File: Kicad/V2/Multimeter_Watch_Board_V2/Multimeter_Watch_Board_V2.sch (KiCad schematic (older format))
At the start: 50 parts, among them J1 S3B-PH-K-S(LF)(SN), J2 S3B-PH-K-S(LF)(SN), J3 S3B-PH-K-S(LF)(SN), J6 51281-1294, J7 Conn_01x11_Female, J8 Conn_01x11_Female, Q1 A03400A N-MOS, U1 PCF85163-SO08, U2 AD8592, Y1 32kHz

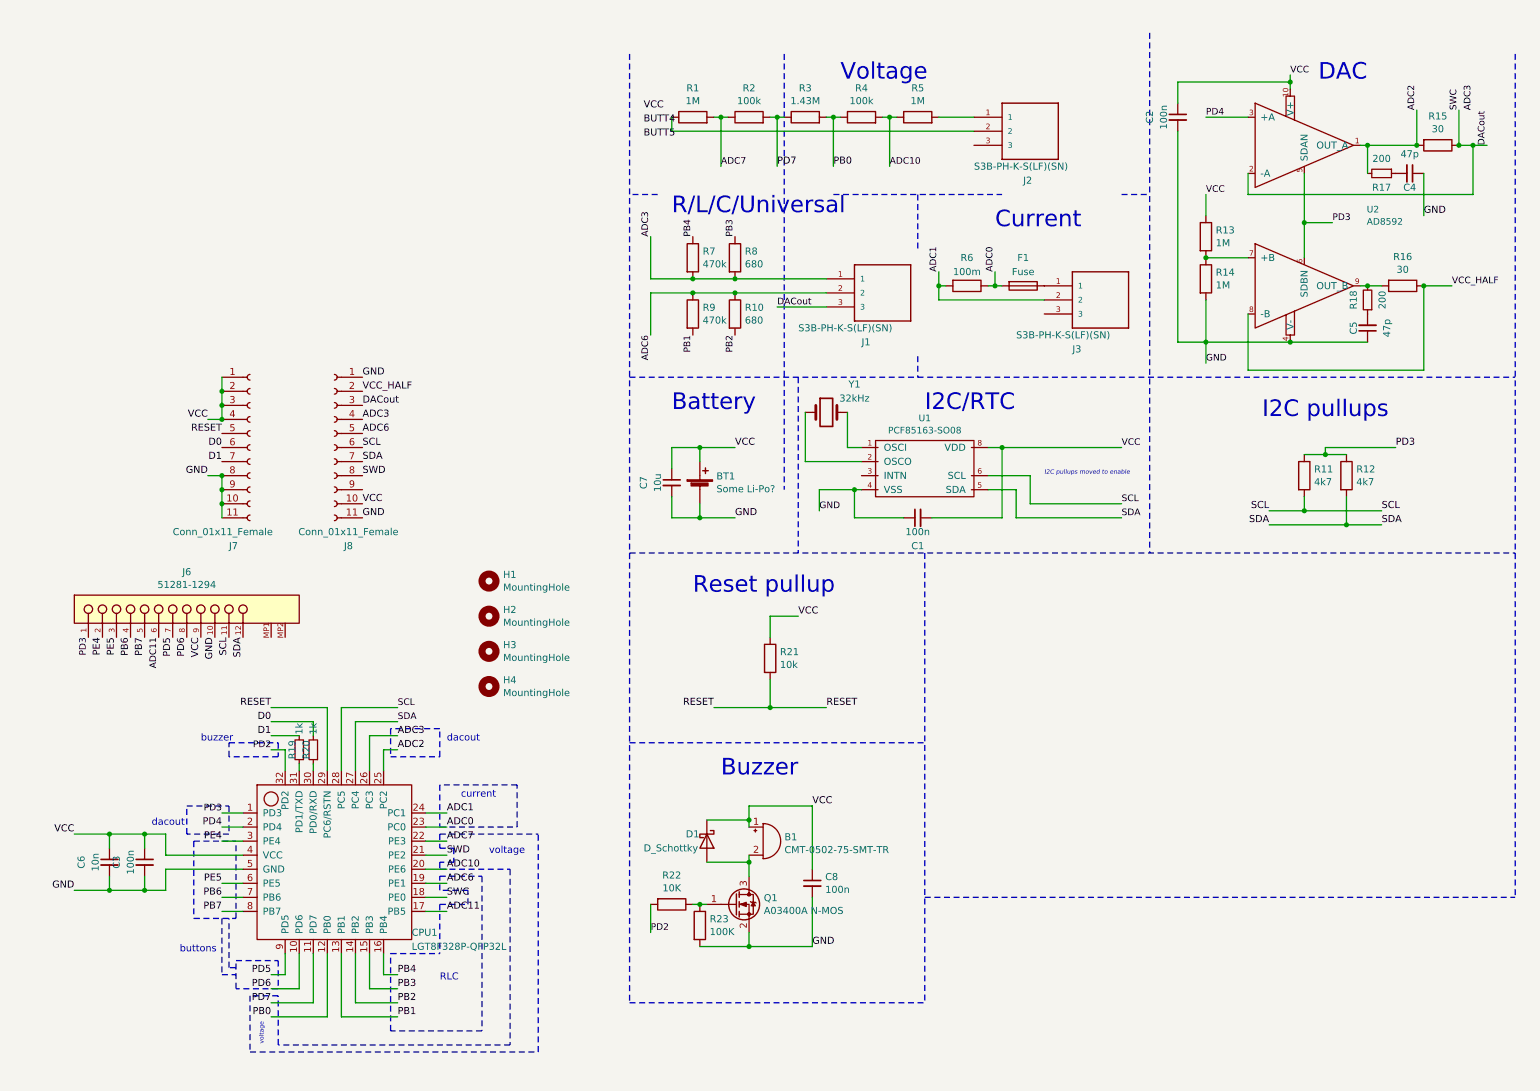
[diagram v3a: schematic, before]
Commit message: clean up schematic
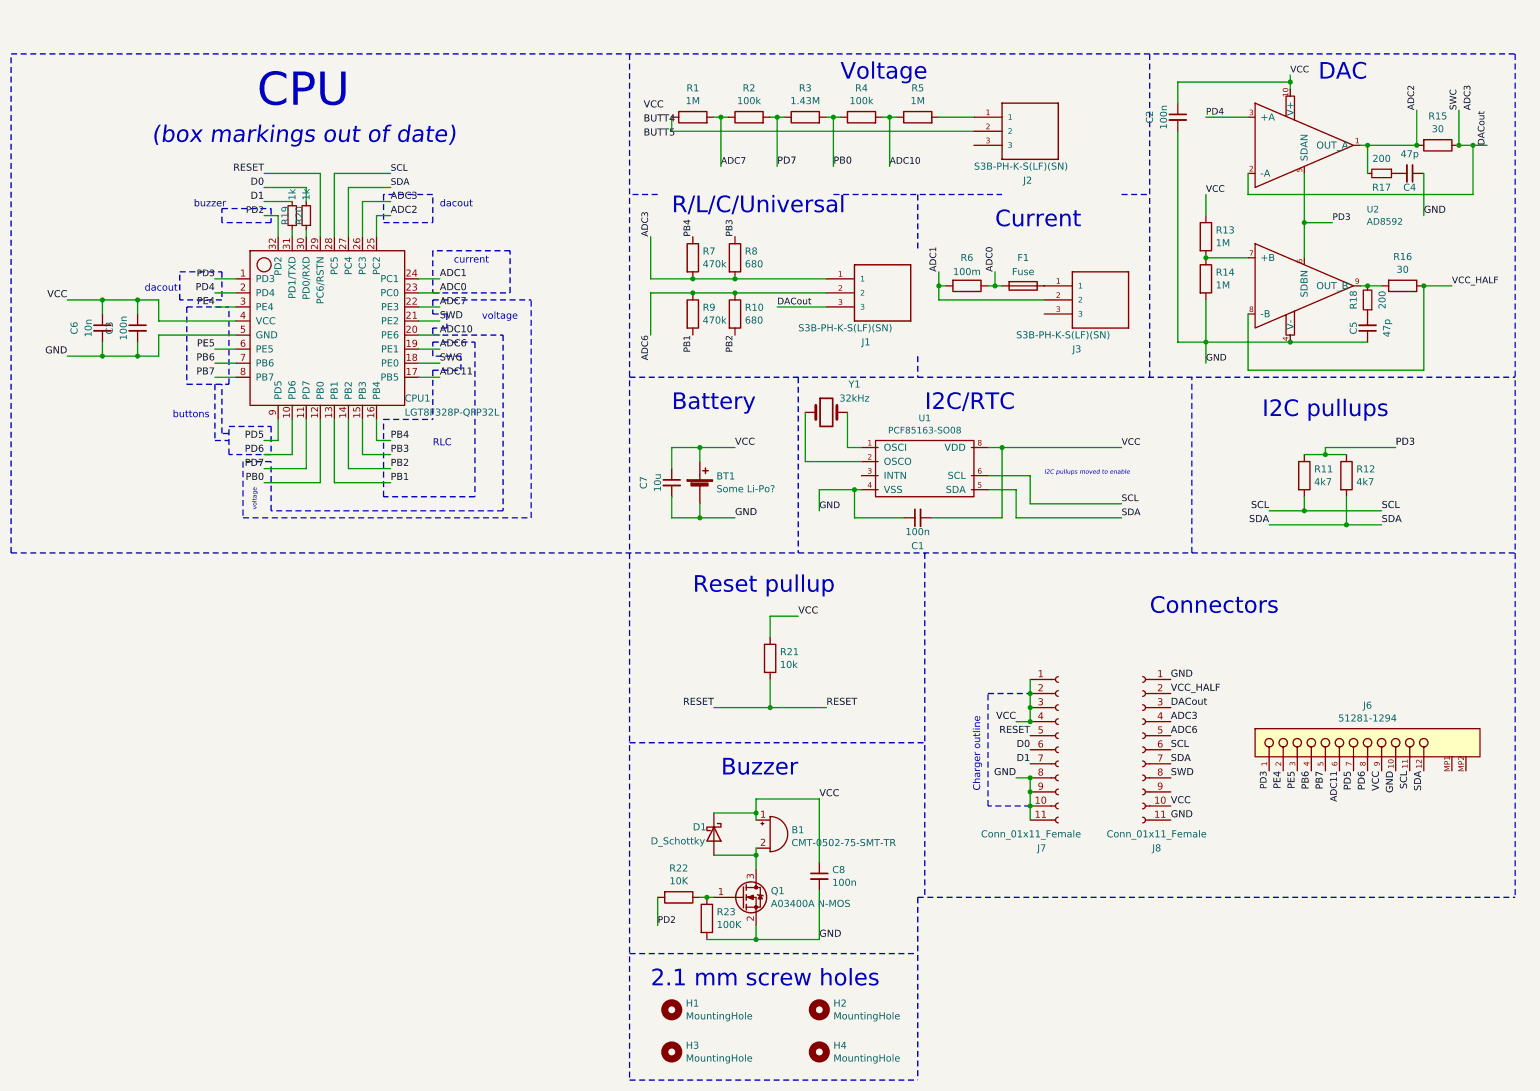
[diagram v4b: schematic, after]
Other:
- note added: "(box markings out of date)"
- note added: "2.1 mm screw holes"
- note added: "CPU"
- note added: "Charger outline"
- note added: "Connectors"
- moved on the sheet: B1, C3, C6, C8, CPU1, D1, H1, H2, H3, H4, J6, J7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

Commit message: displayboard layout for V2
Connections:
- net GND: now also J6.9
- net VCC: no longer J6.9
- net ADC11 renamed PB5
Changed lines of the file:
@@
 ADC10
 Text Label 3550 2800 0    50   ~ 0
-ADC11
+PB5
 Text Label 3550 2200 0    50   ~ 0
 ADC0
@@
 Text Label 9850 5600 3    50   ~ 0
 PB7
-Text Label 10250 5600 3    50   ~ 0
-VCC
 Text Label 9650 5600 3    50   ~ 0
 PE5
@@
 PD3
 Text Label 9950 5600 3    47   ~ 0
-ADC11
+PB5
 Wire Wire Line
 	5800 5800 6250 5800
@@
 Wire Notes Line
 	500  500  11200 500
+Text Label 10250 5600 3    50   ~ 0
+GND
 $EndSCHEMATC

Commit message: females layout improvements, add silkscreen labels for female pins
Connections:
- net DACout: now also J8.6 (Pin_6); no longer J8.3 (Pin_3)
- net SCL: now also J8.8 (Pin_8); no longer J8.6 (Pin_6)
- net SDA: now also J8.9 (Pin_9); no longer J8.7 (Pin_7)
- net SWD: now also J8.7 (Pin_7); no longer J8.8 (Pin_8)
- net VCC: now also J8.2 (Pin_2)
- net VCC_HALF: now also J8.3 (Pin_3); no longer J8.2 (Pin_2)
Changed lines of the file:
@@
 Text Label 8750 4950 0    50   ~ 0
 GND
-Text Label 8750 5050 0    50   ~ 0
+Text Label 8750 5150 0    50   ~ 0
 VCC_HALF
-Text Label 8750 5150 0    50   ~ 0
+Text Label 8750 5450 0    50   ~ 0
 DACout
-Text Label 8750 5650 0    50   ~ 0
+Text Label 8750 5550 0    50   ~ 0
 SWD
 Text Label 8750 5350 0    50   ~ 0
@@
 Text Label 7750 5350 2    50   ~ 0
 RESET
-Text Label 8750 5450 0    50   ~ 0
+Text Label 8750 5650 0    50   ~ 0
 SCL
-Text Label 8750 5550 0    50   ~ 0
+Text Label 8750 5750 0    50   ~ 0
 SDA
 Text Label 9550 5600 3    50   ~ 0
@@
 Text Label 10250 5600 3    50   ~ 0
 GND
+Text Label 8750 5050 0    50   ~ 0
+VCC
 $EndSCHEMATC

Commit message: top board rework (move flex conn up, dedicated display enable)
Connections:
- net PD3: no longer J6.1
- net VCC: now also J6.1
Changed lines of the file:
@@
 Text Label 9550 5600 3    50   ~ 0
 PE4
-Text Label 9450 5600 3    47   ~ 0
-PD3
 Text Label 9950 5600 3    47   ~ 0
 PB5
@@
 Text Label 8750 5050 0    50   ~ 0
 VCC
+Text Label 9450 5600 3    50   ~ 0
+VCC
 $EndSCHEMATC

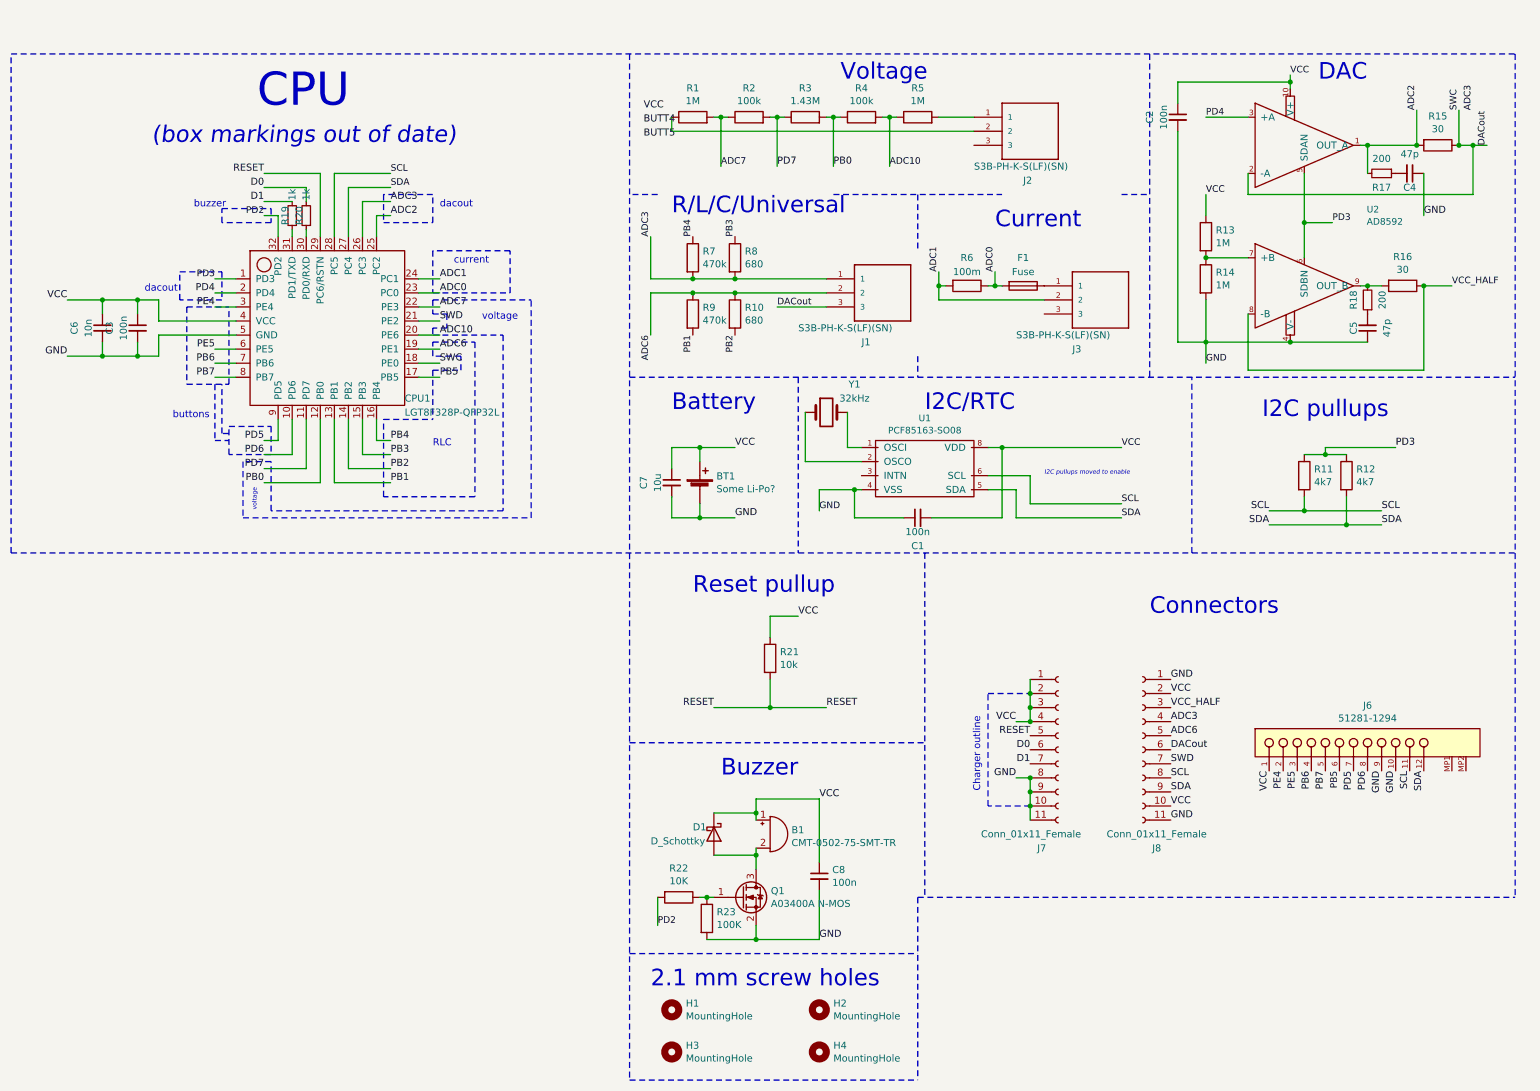
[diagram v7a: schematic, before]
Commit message: add rlc tester protection to schematic
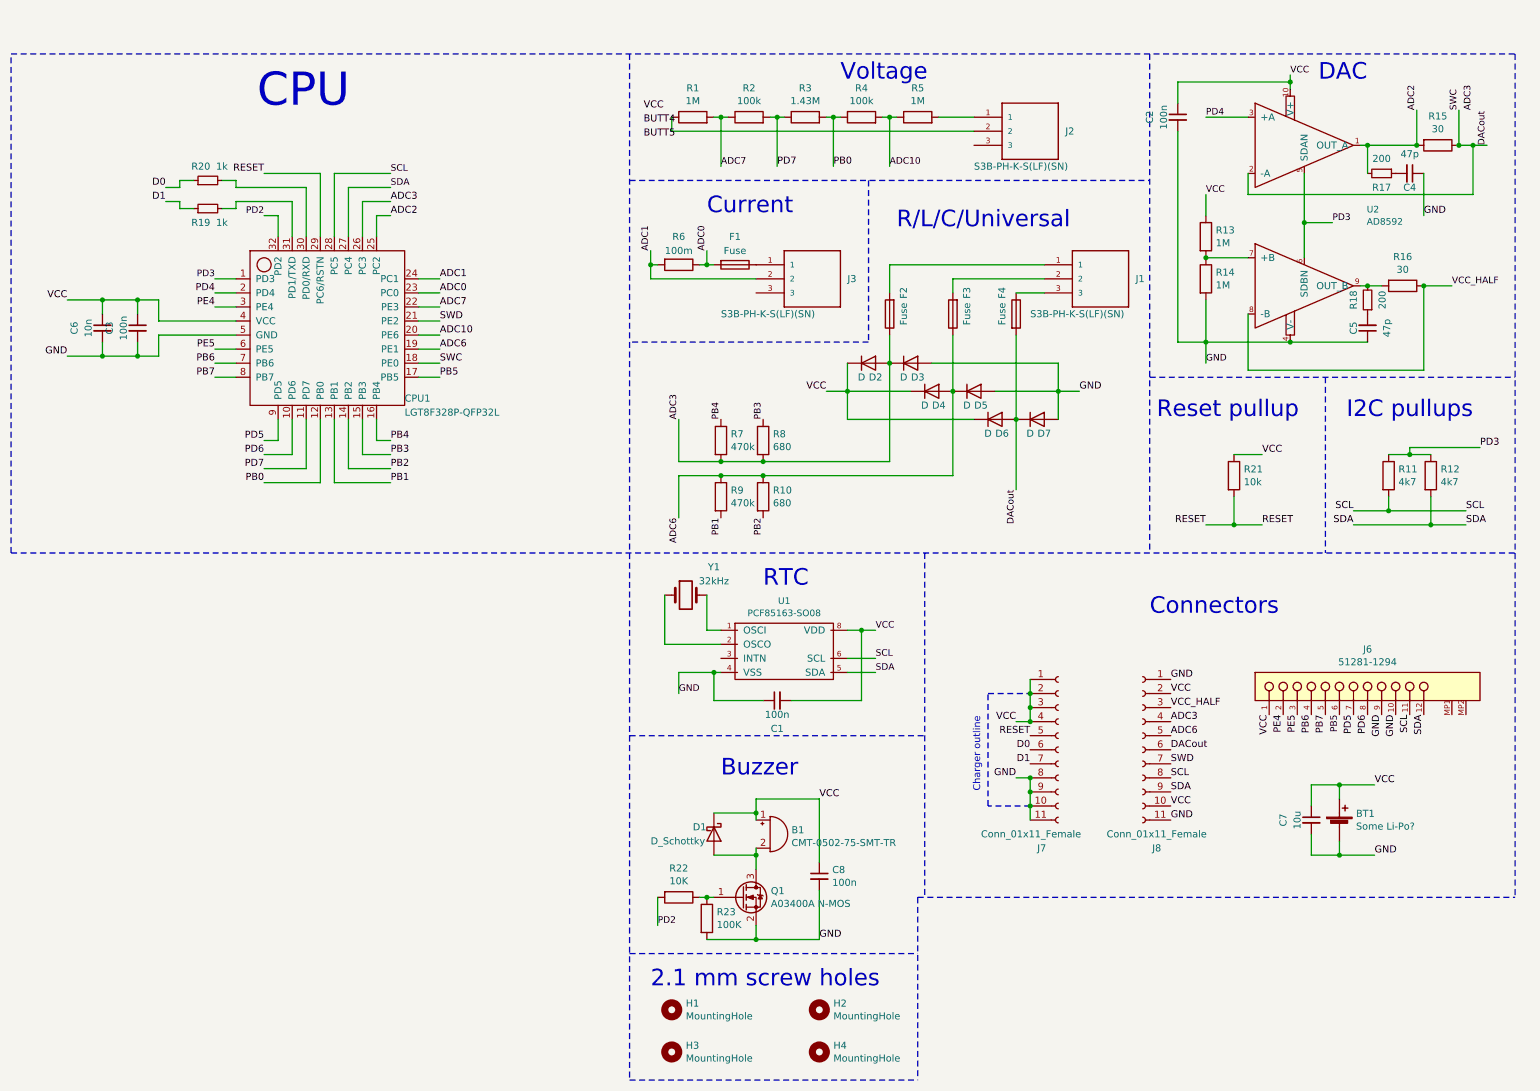
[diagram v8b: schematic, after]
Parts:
- added D2, D3, D4, D5, D6, D7: D, Multimeter_Watch_Custom_Footprints:1408D, symbol Device:D
- added F2, F3, F4: Fuse, Fuse:Fuse_0805_2012Metric_Pad1.15x1.40mm_HandSolder, symbol Device:Fuse
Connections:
- net ADC3: now also D2.2 (A), D3.1 (K), F2.1; no longer J1.1
- net ADC6: now also D4.2 (A), D5.1 (K), F3.1; no longer J1.2
- net D0: now also R20.1; no longer R20.2
- net D1: now also R19.1; no longer R19.2
- net DACout: now also D6.2 (A), D7.1 (K), F4.2; no longer J1.3
- net GND: now also D3.2 (A), D5.2 (A), D7.2 (A)
- net VCC: now also D2.1 (K), D4.1 (K), D6.1 (K)
- net at CPU1.30 (PD0/RXD): now also R20.2; no longer R20.1
- net at CPU1.31 (PD1/TXD): now also R19.2; no longer R19.1
- new net: F2.2, J1.1
- new net: F3.2, J1.2
- new net: F4.1, J1.3
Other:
- note added: "RTC\n"
- note removed: "(box markings out of date)"
- note removed: "Battery"
- note removed: "I2C pullups moved to enable"
- note removed: "I2C/RTC\n"
- note removed: "RLC\n"
- note removed: "buttons\n"
- note removed: "buzzer"
- note removed: "current\n"
- note removed: "dacout"
- note removed: "dacout\n"
- note removed: "voltage\n"
- moved on the sheet: BT1, C1, C7, F1, J1, J3, J6, R10, R11, R12, R19, R20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
